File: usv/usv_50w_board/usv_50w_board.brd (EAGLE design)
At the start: 65 x 30 mm, 27 parts, among them IC1 ADS7828E/250G4, J1 B4B-PH-K-S(LF)(SN), J2 10118193-0001LF, J3 B4B-PH-K-S(LF)(SN), J4 B4B-PH-K-S(LF)(SN), J5 B4B-PH-K-S(LF)(SN), Q1 IRLML6346TRPBF, U2 MPU-9250

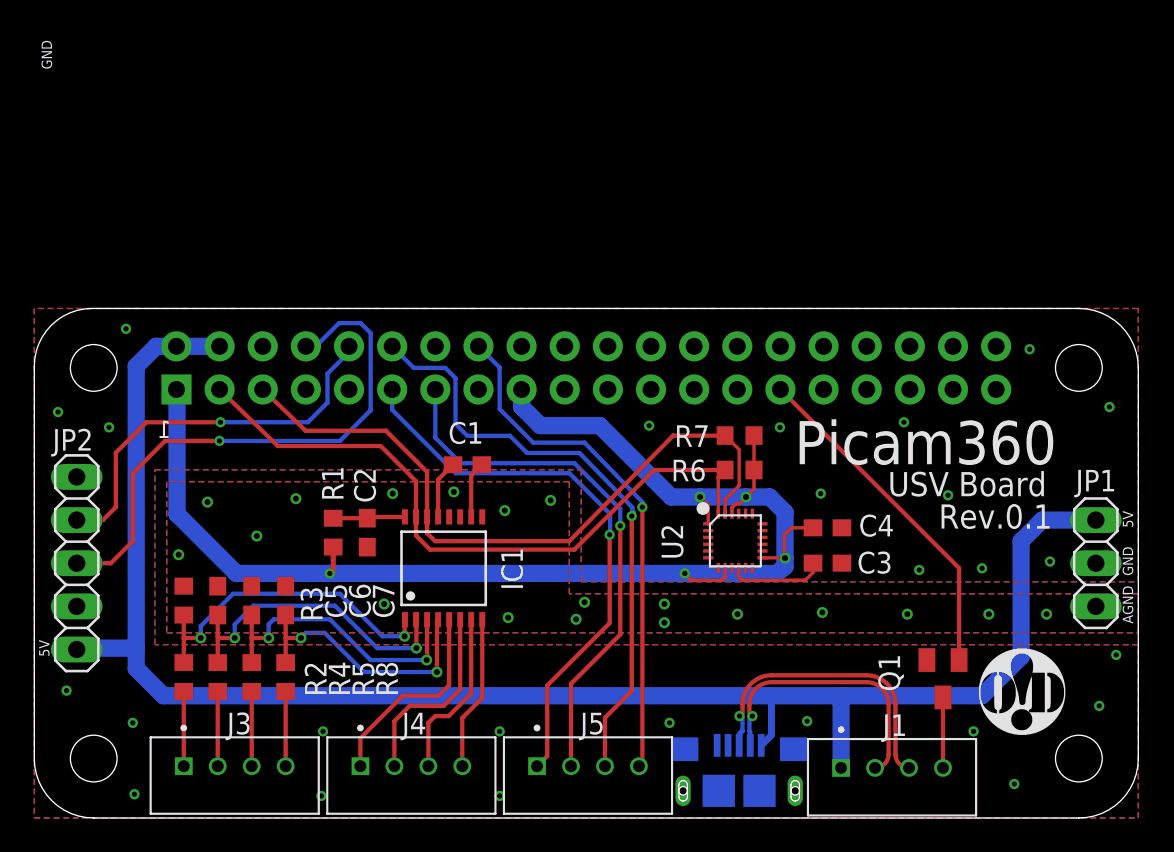
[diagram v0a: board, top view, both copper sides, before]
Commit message: usv 50w rev0.2
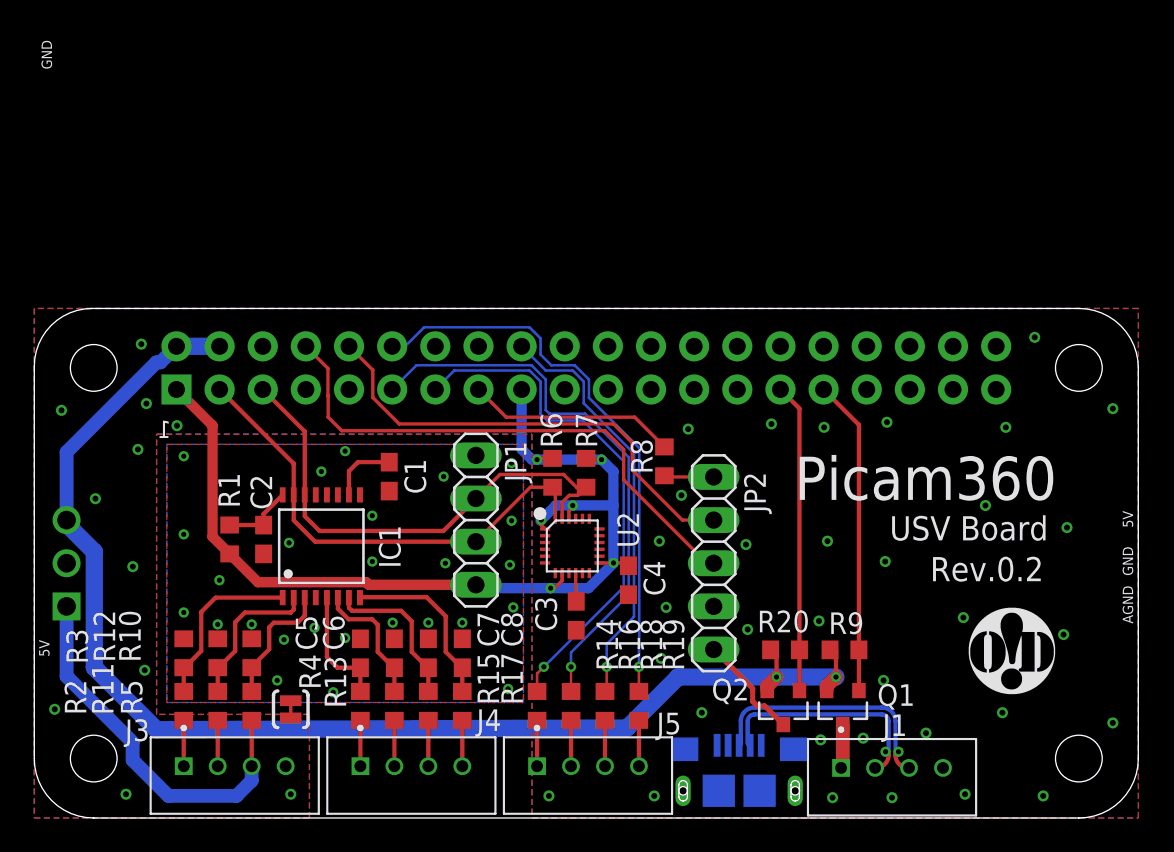
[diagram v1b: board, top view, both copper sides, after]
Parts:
- added C8: 10u, resistor:C0603
- added Q2: (no value), GeekAmmo:SOT23-3
- added R10, R12, R13, R15, R17: 100k, resistor:R0603
- added R11: 500k, resistor:R0603
- added R14, R16, R18, R19, R20, R9: 10k, resistor:R0603
- added SJ1: SOLDERJUMPERTRACE, SparkFun-Retired:SJ_2S-TRACE
- added U1: V7812W-500R, V7812W-500R:CONV_V7812W-500R
- C5, C6, C7: value 4.7u -> 10u
- JP1: device pinhead:1X03 -> pinhead+:1X04
- Q1: value IRLML6346TRPBF -> (none); device openblw:SOT23 -> GeekAmmo:SOT23-3
- R5: value 100k -> 500k
- R8: value 100k -> 10k
- moved JP2 37.5 mm to (40.0, 15.0)
- moved JP1 36.6 mm to (26.0, 17.5), turned to 90 degrees
- moved R8 25.7 mm to (37.1, 21.0)
- moved C3 15.1 mm to (31.9, 11.9), turned to 90 degrees
- moved C4 12.1 mm to (35.0, 14.0), turned to 90 degrees
- moved R6 11.0 mm to (30.5, 20.3), turned to 90 degrees
- moved U2 9.60 mm to (31.7, 16.0)
- moved R7 9.30 mm to (32.5, 20.3), turned to 90 degrees
- moved C5 8.95 mm to (19.2, 9.70), turned to 90 degrees
- moved C6 8.95 mm to (21.2, 9.70), turned to 90 degrees
- moved C7 8.95 mm to (23.2, 9.70), turned to 90 degrees
- moved R4 8.57 mm to (19.2, 6.60)
- moved IC1 7.32 mm to (16.9, 16.0)
- moved Q1 6.14 mm to (47.6, 6.50)
- moved C2 6.11 mm to (13.5, 16.4)
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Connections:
- net 12VBAT_SENSE renamed SOLAR_SENSE
- net 12VBAT_SRC renamed SOLAR_V
- removed net RX1_SENSE: C5.2, IC1.2, R4.1
- removed net RX1_SRC: J3.2, R4.2
- removed net RX2_SENSE: C6.2, IC1.3, R5.1
- removed net RX2_SRC: J3.3, R5.2
- removed net RX3_SENSE: C7.2, IC1.4, R8.1
- removed net RX3_SRC: J3.4, R8.2
- new net 12V: J3.3, R5.2, U1.1
- new net 12V_SENSE: IC1.3, R10.1, R5.1
- new net BAT_SENSE: IC1.2, R11.1, R12.1
- new net BAT_V: J3.2, R11.2
- new net EXT1_V: J4.1, R4.2
- new net EXT2_V: J4.2, R13.2
- new net EXT3_V: J4.3, R15.2
- new net EXT4_V: J4.4, R17.2
- new net GPS_1PPS: JP2.5, R8.2
- new net GPS_5V: JP2.1, Q2.3
- new net GPS_ENABLE: Q2.1, R20.2, U$3.29
- new net N$2: R8.1, U$3.15
- new net N$3: R14.1, U$3.13
- new net N$5: R16.1, U$3.11
- new net N$7: R19.2, U$3.12
- new net RESERVED: IC1.4
- new net USB_5V: J1.1, Q1.3
- net +3V3: now also JP1.1
- net +5V: now also Q1.2, Q2.2, R20.1, R9.1, U1.3; no longer J1.1, J2.1, JP1.1, JP2.1
- net AGND: now also C5.2, C6.2, C7.2, C8.2, JP1.4, R10.2, R12.2, SJ1.1; no longer C5.1, C6.1, C7.1, JP1.3
- net EXT1_SENSE: now also C5.1, R4.1; no longer J4.1
- net EXT2_SENSE: now also C6.1, R13.1; no longer J4.2
- net EXT3_SENSE: now also C7.1, R15.1; no longer J4.3
- net EXT4_SENSE: now also C8.1, R17.1; no longer J4.4
- net GND: now also J1.4, J3.4, SJ1.2, U1.2; no longer JP1.2, Q1.2
- net N$6: now also R18.2, U$3.18; no longer J1.4, Q1.3
- net PWM1: now also R14.2; no longer U$3.11
- net PWM2: now also R16.2; no longer U$3.13
- net PWM3: now also R18.1; no longer U$3.12
- net PWM4: now also R19.1; no longer U$3.16
- net TWI_SCL: now also JP1.3
- net TWI_SDA: now also JP1.2
- net USB_ENABLE: now also R9.2, U$3.31; no longer U$3.29
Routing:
- net N$7: track 0.00 -> 33.5 mm, vias 0 -> 1
- net PWM3: track 35.7 -> 2.70 mm, vias 1 -> 0
- net N$5: track 0.00 -> 33.0 mm, vias 0 -> 1
- net PWM1: track 33.4 -> 2.70 mm, vias 1 -> 0
- net N$3: track 0.00 -> 30.5 mm, vias 0 -> 1
- net PWM2: track 31.9 -> 2.70 mm, vias 1 -> 0
- net PWM4: track 30.6 -> 2.70 mm, vias 1 -> 0
- net 12V: track 0.00 -> 22.5 mm
- net +3V3: track 83.5 -> 61.2 mm, vias 5 -> 6
- net +5V: track 99.6 -> 77.3 mm, vias 0 -> 2
- net N$6: track 4.15 -> 24.7 mm, vias 0 -> 1
- net RX1_SENSE: track 18.5 -> 0.00 mm, vias 2 -> 0
- net GPS_ENABLE: track 0.00 -> 18.2 mm
- net RX2_SENSE: track 17.4 -> 0.00 mm, vias 2 -> 0
- net RX3_SENSE: track 16.0 -> 0.00 mm, vias 2 -> 0
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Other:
- board text added: "Rev.0.2"
- board text removed: "Rev.0.1"

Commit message: usv 50w 0.3
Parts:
- removed Q1, Q2: (no value), GeekAmmo:SOT23-3
- removed R20, R8, R9: 10k, resistor:R0603
- added C10, C11, C13: 10u, resistor:C0603
- added C12, C14, C9: 100n, resistor:C0603
- added U$1: AP2166S, diodes-inc:SO08
- JP1: device pinhead+:1X04 -> pinhead+:1X05
- moved C4 27.5 mm to (7.68, 11.1)
- moved C3 26.2 mm to (5.71, 11.1)
- moved R6 24.9 mm to (5.61, 19.7)
- moved R7 24.9 mm to (7.58, 19.7)
- moved U2 24.9 mm to (6.78, 15.4)
- moved R19 4.97 mm to (33.5, 11.1)
- moved R14 4.88 mm to (31.5, 11.1)
- moved JP2 3.73 mm to (36.3, 15.0)
- moved JP1 3.73 mm to (28.7, 15.0)
- moved LOGO1 3.41 mm to (60.5, 11.6)
- moved IC1 2.76 mm to (18.9, 17.9)
- moved C2 2.44 mm to (15.5, 17.8)
- moved R1 2.44 mm to (13.5, 17.8)
- moved R10 2.44 mm to (14.8, 11.1)
- moved R12 2.44 mm to (12.8, 11.1)
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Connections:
- removed net N$2: R8.1, U$3.15
- removed net RESERVED: IC1.4
- removed net USB_D_N: J1.2, J2.2
- removed net USB_D_P: J1.3, J2.3
- new net D_N: J1.3, J2.2
- new net D_P: J1.2, J2.3
- net +3V3: now also JP1.2; no longer JP1.1, U$3.17
- net +5V: now also C10.1, C14.1, U$1.7; no longer Q1.2, Q2.2, R20.1, R9.1
- net AGND: no longer JP1.4
- net GND: now also C10.2, C11.2, C12.2, C13.2, C14.2, C9.2, IC1.4, J1.1, JP1.5, U$1.6; no longer J1.4
- net GPS_1PPS: now also U$3.15; no longer R8.2
- net GPS_5V: now also C12.1, C13.1, JP1.1, U$1.5; no longer Q2.3
- net GPS_ENABLE: now also U$1.4; no longer Q2.1, R20.2
- net TWI_SCL: now also JP1.4; no longer JP1.3
- net TWI_SDA: now also JP1.3; no longer JP1.2
- net USB_5V: now also C11.1, C9.1, J1.4, U$1.8; no longer J1.1, Q1.3
- net USB_ENABLE: now also U$1.1; no longer Q1.1, R9.2
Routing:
- net USB_D_P: track 14.7 -> 0.00 mm, vias 1 -> 0
- net USB_5V: track 2.59 -> 16.9 mm
- net USB_ENABLE: track 18.6 -> 4.92 mm
- net USB_D_N: track 13.6 -> 0.00 mm, vias 1 -> 0
- net GPS_ENABLE: track 18.2 -> 4.67 mm
- net GPS_5V: track 6.38 -> 19.8 mm
- net GND: track 0.00 -> 13.3 mm, vias 44 -> 34
- net D_N: track 0.00 -> 13.3 mm, vias 0 -> 1
- net D_P: track 0.00 -> 13.3 mm, vias 0 -> 1
- net N$2: track 12.4 -> 0.00 mm
- net TWI_SDA: track 28.5 -> 40.0 mm, vias 0 -> 1
- net GPS_1PPS: track 2.91 -> 12.3 mm
- net N$3: track 30.5 -> 23.7 mm
- net N$7: track 33.5 -> 28.4 mm
- net +3V3: track 61.2 -> 65.8 mm, vias 6 -> 5
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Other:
- board text added: "Rev.0.3"
- board text removed: "AGND"
- board text removed: "GND"
- board text removed: "Rev.0.2"
